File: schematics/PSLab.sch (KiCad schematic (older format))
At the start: 79 parts, among them J1 Programmer, J10 GND, J11 Vbus, J13 D+, J14 D-, J15 External Power, J16 I2C-2, J2 DoublePins, J5 Bluetooth, J6 I2C-1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

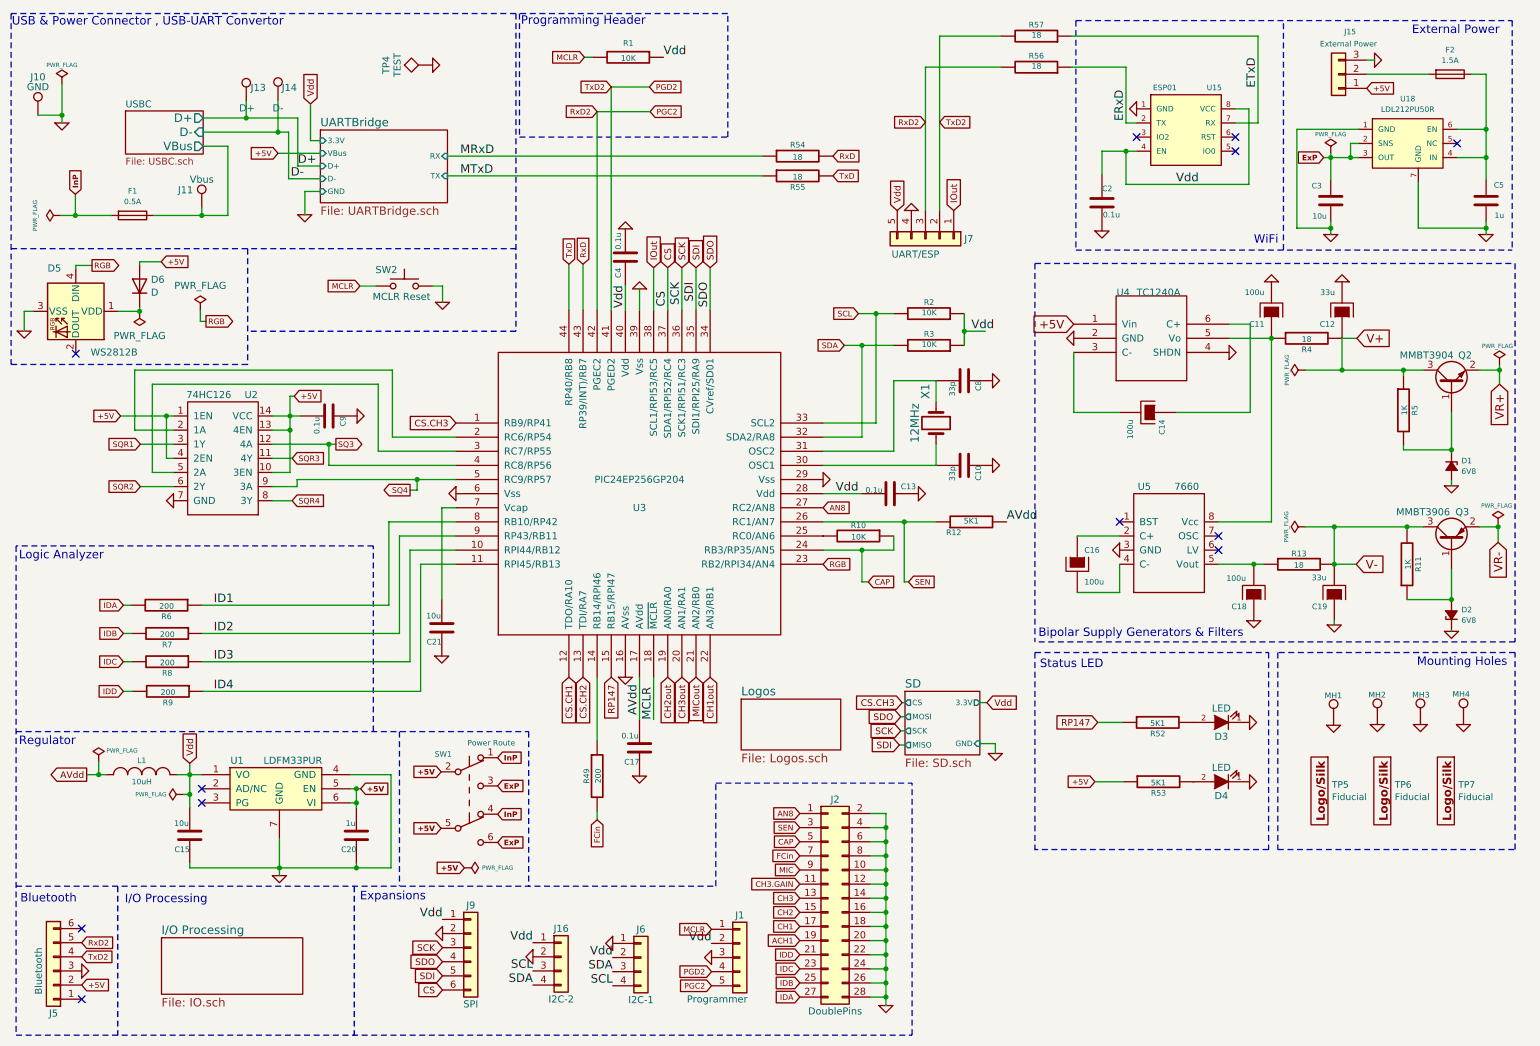
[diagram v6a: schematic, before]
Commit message: feat: bom generator and updated project to support bom generator
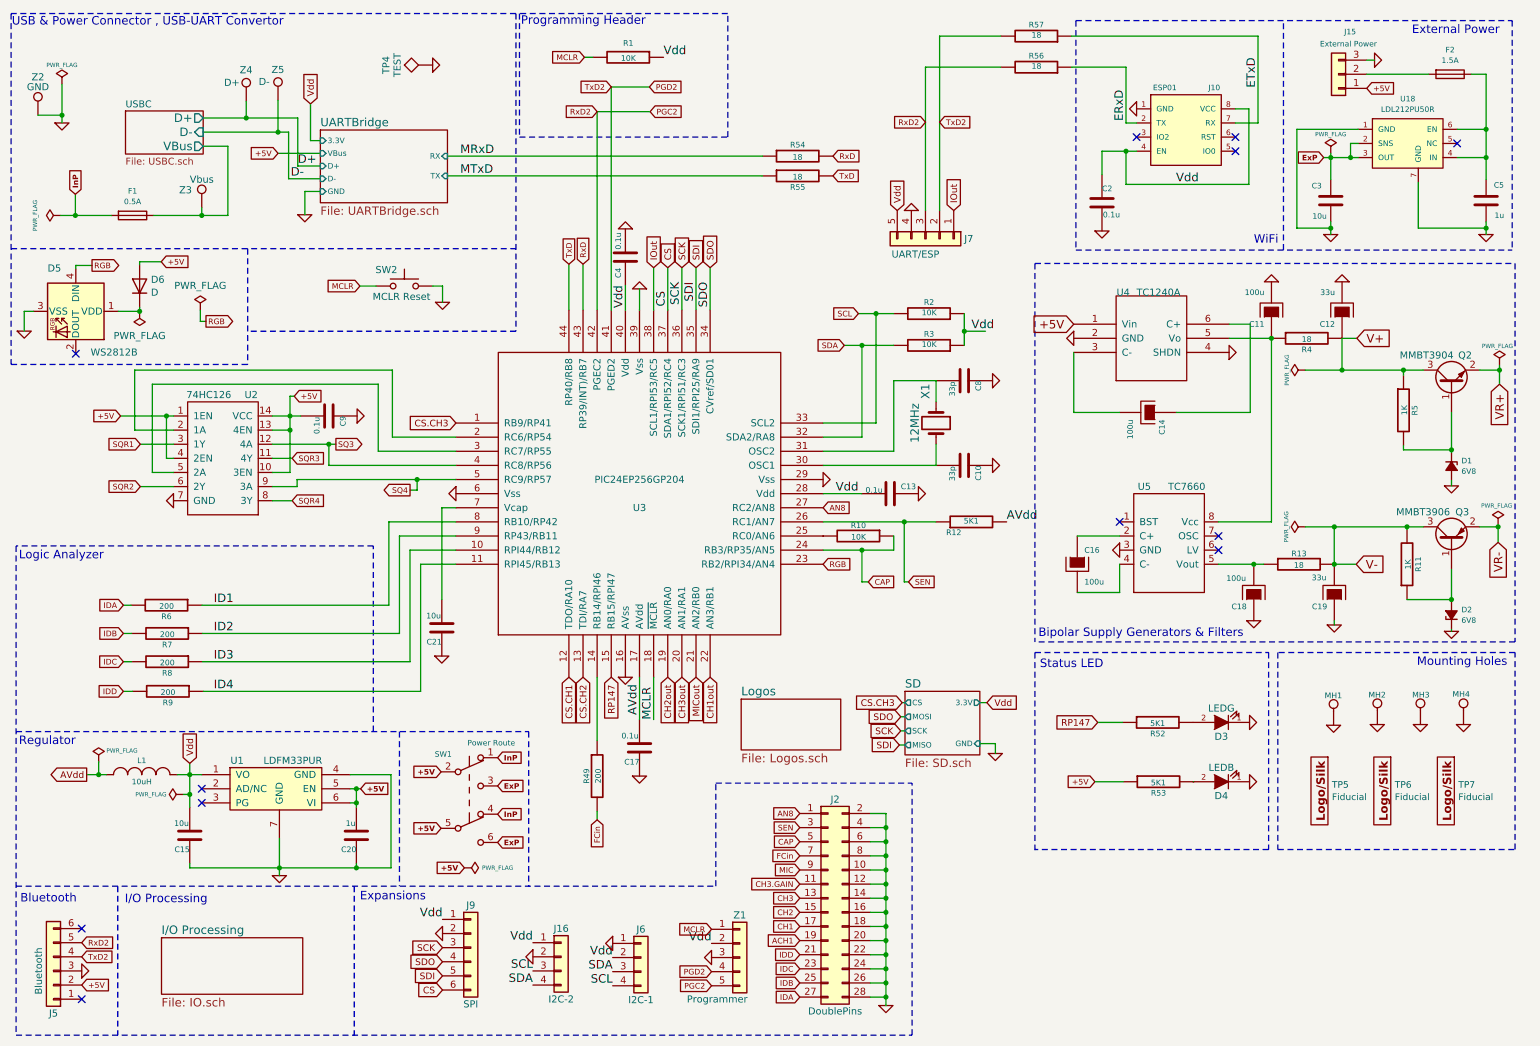
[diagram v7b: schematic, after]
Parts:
- C10, C8: Description (none) -> 16V 10%; Mfr No. (none) -> VJ0603A330JXJPW1BC; PartNumber (none) -> VJ0603A330JXJPW1BC; Price (none) -> 0.26
- C11, C14, C16, C18: Description (none) -> Tantalum 16V 6032-28; Mfr No. (none) -> F931C107KCC; PartNumber (none) -> F931C107KCC; Price (none) -> 1.29
- C12, C19: Description (none) -> Tantalum 16V 3528-21; Mfr No. (none) -> 293D336X9016B2TE3; PartNumber (none) -> 293D336X9016B2TE3; Price (none) -> 0.81
- C13, C17, C2, C4, C9: Description (none) -> 16V 10%; Mfr No. (none) -> C0603C104J4RACTU; PartNumber (none) -> C0603C104J4RACTU; Price (none) -> 0.15
- C15, C21, C3: Description (none) -> 16V 20%; Mfr No. (none) -> EMK107BC6106MA-T; PartNumber (none) -> EMK107BC6106MA-T; Price (none) -> 0.46
- C20, C5: Description (none) -> 16V 20%; Mfr No. (none) -> 0603YD105KAT2A; PartNumber (none) -> 0603YD105KAT2A; Price (none) -> 0.18
- D1, D2: Description (none) -> 6.8V Zener; Mfr No. (none) -> BZV55B6V8 L1; PartNumber (none) -> BZV55B6V8 L1; Price (none) -> 0.23
- D3: value LED -> LEDG; Description (none) -> Green 0805; Mfr No. (none) -> HSMQ-C170-T0000; PartNumber (none) -> HSMQ-C170-T0000; Price (none) -> 0.94
- D4: value LED -> LEDB; Description (none) -> Blue 0805; Mfr No. (none) -> HSMR-C170-R0000; PartNumber (none) -> HSMR-C170-R0000; Price (none) -> 0.85
- D5: Description (none) -> RGB LED with integrated controller; Mfr No. (none) -> WS2812B; PartNumber (none) -> WS2812B; Price (none) -> 3.35
- D6: Description (none) -> General Purpose diode; Mfr No. (none) -> LL4448 L0; PartNumber (none) -> LL4448 L0; Price (none) -> 0.11
- F1: Description (none) -> Hold 250mA, Trip 500mA; Mfr No. (none) -> 0ZCJ0025FF2E; PartNumber (none) -> 0ZCJ0025FF2E; Price (none) -> 0.11
- F2: Description (none) -> Hold 1A, Trip 1.8A; Mfr No. (none) -> 0ZCJ0100FF2E; PartNumber (none) -> 0ZCJ0100FF2E; Price (none) -> 0.17
- J10: renamed from U15; footprint Custom_Components:ESP-01 -> PSLab:ESP-01; Description (none) -> Straight female 2.54 mm 2row; Mfr No. (none) -> SSW-104-01-T-D; PartNumber (none) -> SSW-104-01-T-D; Price (none) -> 0.98
- J15: Description (none) -> Straight female 2.54 mm 1row; Mfr No. (none) -> SSW-103-01-T-S; PartNumber (none) -> SSW-103-01-T-S; Price (none) -> 0.5
- J16, J6: Description (none) -> Straight female 2.54 mm 1row; Mfr No. (none) -> SSW-104-01-T-S; PartNumber (none) -> SSW-104-01-T-S; Price (none) -> 0.63
- J2: Description (none) -> Straight female 2.54 mm 2row; Mfr No. (none) -> SSW-114-01-T-D; PartNumber (none) -> SSW-114-01-T-D; Price (none) -> 2.28
- J5, J9: Description (none) -> Straight female 2.54 mm 1row; Mfr No. (none) -> SSW-106-01-T-S; PartNumber (none) -> SSW-106-01-T-S; Price (none) -> 0.68
- J7: Description (none) -> Straight female 2.54 mm 1row; Mfr No. (none) -> SSW-105-01-T-S; PartNumber (none) -> SSW-105-01-T-S; Price (none) -> 0.65
- L1: Description (none) -> 300-500 mA Shielded; Mfr No. (none) -> MLZ1608N100LT000; PartNumber (none) -> MLZ1608N100LT000; Price (none) -> 0.17
- MH1, MH2, MH3, MH4: Description (none) -> M3 Nut - 3.2mm_M3.5_DIN965; Mfr No. (none) -> 9774030360R; PartNumber (none) -> 9774030360R; Price (none) -> 2.86
- Q2: Description (none) -> 45V Vce, 0.8A Ic, NPN, SOT-23; Mfr No. (none) -> MMBT3904,215; PartNumber (none) -> MMBT3904,215; Price (none) -> 0.1
- Q3: Description (none) -> 45V Vce, 0.8A Ic, PNP, SOT-23; Mfr No. (none) -> MMBT3906-7-F; PartNumber (none) -> MMBT3906-7-F; Price (none) -> 0.11
- R1, R10, R2, R3: Description (none) -> 1/16W 5%; Mfr No. (none) -> RR0816P-103-D; PartNumber (none) -> RR0816P-103-D; Price (none) -> 0.12
- R11, R5: Description (none) -> 1/16W 5%; Mfr No. (none) -> RR0816P-102-D; PartNumber (none) -> RR0816P-102-D; Price (none) -> 0.12
- R12, R52, R53: Description (none) -> 1/16W 5%; Mfr No. (none) -> RR0816P-512-D; PartNumber (none) -> RR0816P-512-D; Price (none) -> 0.1
- R13, R4, R54, R55, R56, R57: Description (none) -> 1/16W 5%; Mfr No. (none) -> RR0816Q-180-D; PartNumber (none) -> RR0816Q-180-D; Price (none) -> 0.1
- R49, R6, R7, R8, R9: Description (none) -> 1/16W 5%; Mfr No. (none) -> RR0816P-201-D; PartNumber (none) -> RR0816P-201-D; Price (none) -> 0.1
- SW1: Description (none) -> Slide Switches DPDT THRU HOLE; PartNumber (none) -> JS202011CQN; Price (none) -> 0.43
- SW2: Description (none) -> Tactile Switches SPST SMD; Mfr No. (none) -> B3U-1000P; PartNumber (none) -> B3U-1000P; Price (none) -> 0.56
- U1: Description (none) -> DFN-6-1EP_3x3mm_Pitch0.95mm; Mfr No. (none) -> LDFM33PUR; PartNumber (none) -> LDFM33PUR; Price (none) -> 0.72
- U18: Description (none) -> DFN-6-1EP_3x3mm_Pitch0.95mm; Mfr No. (none) -> LDL212PU50R; PartNumber (none) -> LDL212PU50R; Price (none) -> 0.51
- U2: Description (none) -> SOIC 14; Mfr No. (none) -> 74HC126D(BJ); PartNumber (none) -> 74HC126D(BJ); Price (none) -> 0.42
- U3: Description (none) -> TQFP 44; Mfr No. (none) -> PIC24EP256GP204-I/PT; PartNumber (none) -> PIC24EP256GP204-I/PT; Price (none) -> 3.35
- U4: Description (none) -> SOT-23-6; Mfr No. (none) -> TC1240AECHTR; PartNumber (none) -> TC1240AECHTR; Price (none) -> 0.82
- U5: value 7660 -> TC7660; Description (none) -> SOIC 8; Mfr No. (none) -> TC7660SEOA713; PartNumber (none) -> TC7660SEOA713; Price (none) -> 0.90
- X1: Description (none) -> 18pF 30ppm; Mfr No. (none) -> ABM3-12.000MHZ-D2Y-T; PartNumber (none) -> ABM3-12.000MHZ-D2Y-T; Price (none) -> 0.78
- renumbered J1 to Z1, J10 to Z2, J11 to Z3, J13 to Z4, J14 to Z5

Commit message: refactor: corrected IC annotation order
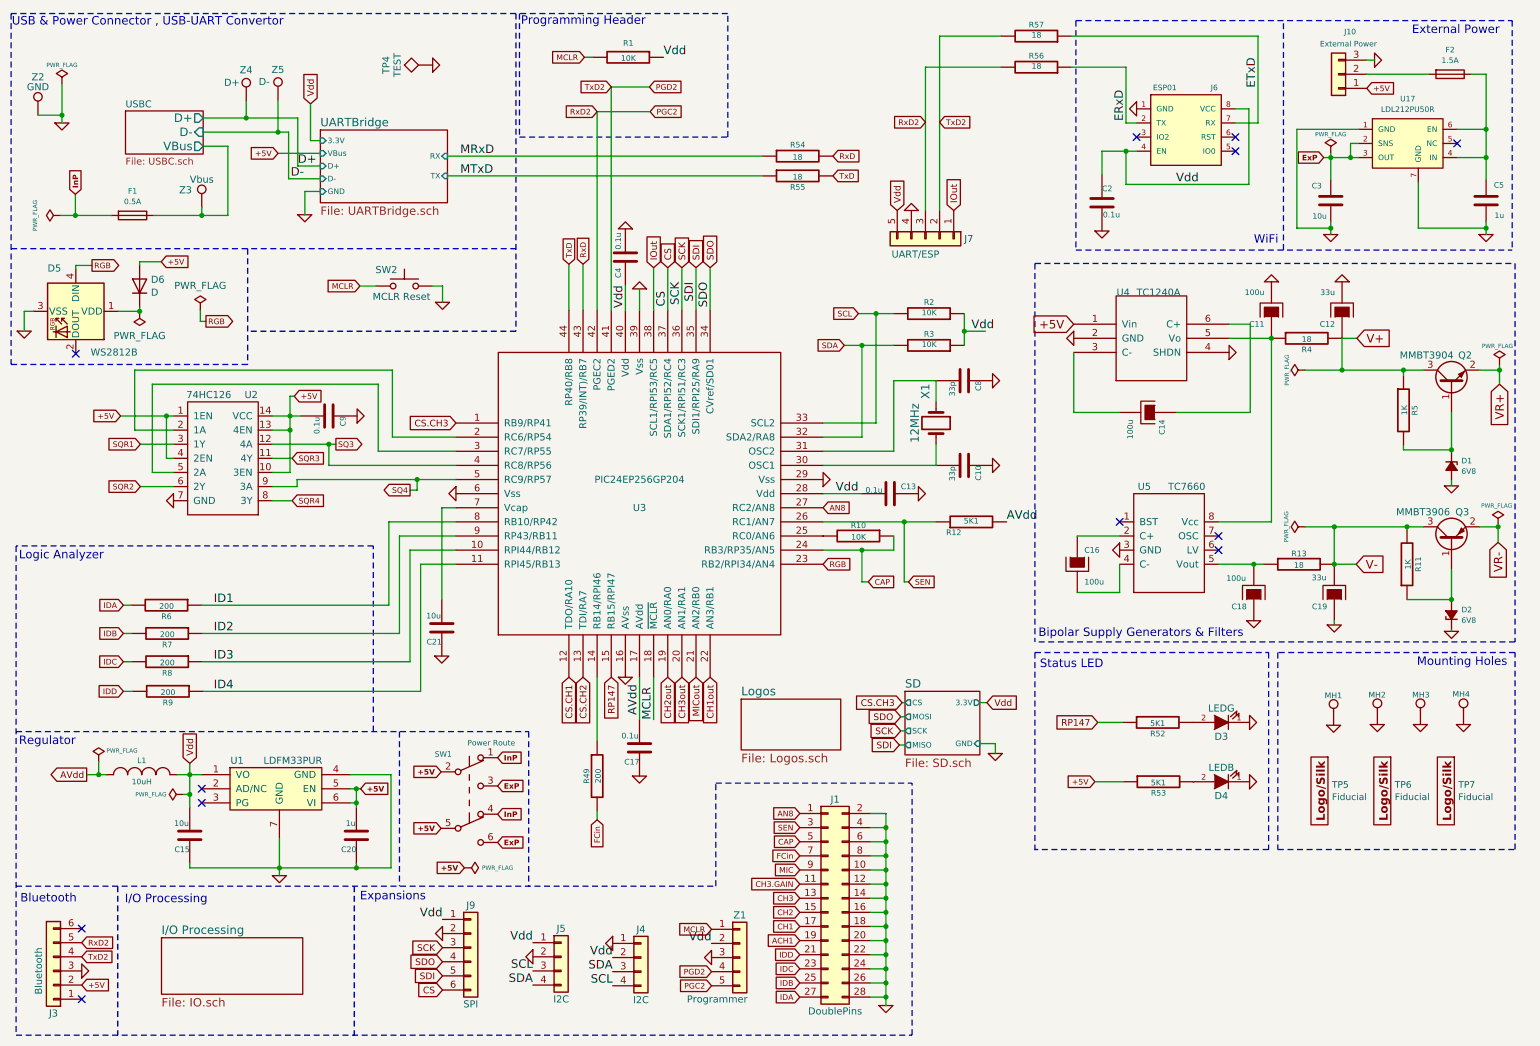
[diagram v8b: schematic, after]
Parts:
- J4: renamed from J6; value I2C-1 -> I2C
- J5: renamed from J16; value I2C-2 -> I2C
- U2: footprint Housings_SOIC:SOIC-14_3.9x8.7mm_Pitch1.27mm -> Package_SO:SOIC-14_3.9x8.7mm_P1.27mm
- U3: footprint Housings_QFP:TQFP-44_10x10mm_Pitch0.8mm -> Package_QFP:TQFP-44_10x10mm_P0.8mm
- U4: footprint TO_SOT_Packages_SMD:SOT-23-6 -> Package_TO_SOT_SMD:SOT-23-6
- U5: footprint Housings_SOIC:SOIC-8_3.9x4.9mm_Pitch1.27mm -> Package_SO:SOIC-8_3.9x4.9mm_P1.27mm
- renumbered J2 to J1, J15 to J10, J5 to J3, J10 to J6, U18 to U17
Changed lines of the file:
@@
 F 0 "U4" H 8375 3125 50  0000 C CNN
 F 1 "TC1240A" H 8625 3125 50  0000 C CNN
-F 2 "TO_SOT_Packages_SMD:SOT-23-6" H 8575 3000 50  0001 C CNN
+F 2 "Package_TO_SOT_SMD:SOT-23-6" H 8575 3000 50  0001 C CNN
 F 3 "https://eu.mouser.com/datasheet/2/268/21516c-4387.pdf" H 8575 2600 50  0001 C CNN
 F 4 "SOT-23-6" H 8575 2800 50  0001 C CNN "Description"
@@
 F 0 "U5" H 8525 4650 50  0000 C CNN
 F 1 "TC7660" H 8825 4650 50  0000 C CNN
-F 2 "Housings_SOIC:SOIC-8_3.9x4.9mm_Pitch1.27mm" H 8700 4250 50  0001 C CNN
+F 2 "Package_SO:SOIC-8_3.9x4.9mm_P1.27mm" H 8700 4250 50  0001 C CNN
 F 3 "https://eu.mouser.com/datasheet/2/268/21467B-1180369.pdf" H 8700 4250 50  0001 C CNN
 F 4 "SOIC 8" H 8700 4250 50  0001 C CNN "Description"
@@
 F 0 "U2" H 2200 4300 50  0000 C CNN
 F 1 "74HC126" H 1900 4300 50  0000 C CNN
-F 2 "Housings_SOIC:SOIC-14_3.9x8.7mm_Pitch1.27mm" V 1975 3575 50  0001 C CNN
+F 2 "Package_SO:SOIC-14_3.9x8.7mm_P1.27mm" V 1975 3575 50  0001 C CNN
 F 3 "https://eu.mouser.com/datasheet/2/408/74HC126D_datasheet_en_20160804-959200.pdf" V 1925 3575 50  0001 C CNN
 F 4 "SOIC 14" H 1800 3750 50  0001 C CNN "Description"
@@
 F 0 "U3" H 4950 3800 50  0000 C CNN
 F 1 "PIC24EP256GP204" H 4950 4000 50  0000 C CNN
-F 2 "Housings_QFP:TQFP-44_10x10mm_Pitch0.8mm" H 4950 3900 50  0001 C CNN
+F 2 "Package_QFP:TQFP-44_10x10mm_P0.8mm" H 4950 3900 50  0001 C CNN
 F 3 "https://eu.mouser.com/datasheet/2/268/70000657H-277982.pdf" H 4950 3900 50  0001 C CNN
 F 4 "TQFP 44" H 4950 3900 50  0001 C CNN "Description"
@@
 MCLR
 $Comp
-L PSLab-rescue:Conn_01x04 J6
+L PSLab-rescue:Conn_01x04 J4
 U 1 1 5A584DF9
 P 4960 7185
-F 0 "J6" H 4960 7385 50  0000 C CNN
-F 1 "I2C-1" H 4960 6885 50  0000 C CNN
+F 0 "J4" H 4960 7385 50  0000 C CNN
+F 1 "I2C" H 4960 6885 50  0000 C CNN
 F 2 "Pin_Headers:Pin_Header_Straight_1x04_Pitch2.54mm" H 4960 7185 50  0001 C CNN
 F 3 "https://eu.mouser.com/datasheet/2/527/ssw_th-1507658.pdf" H 4960 7185 50  0001 C CNN
@@
 Text Label 5460 7085 2    60   ~ 0
 Vdd
-$Comp
-L PSLab-rescue:Conn_01x04 J16
-U 1 1 5AD47B2C
-P 4395 7180
-F 0 "J16" H 4395 7380 50  0000 C CNN
-F 1 "I2C-2" H 4395 6880 50  0000 C CNN
-F 2 "Pin_Headers:Pin_Header_Straight_1x04_Pitch2.54mm" H 4395 7180 50  0001 C CNN
-F 3 "https://eu.mouser.com/datasheet/2/527/ssw_th-1507658.pdf" H 4395 7180 50  0001 C CNN
-F 4 "Straight female 2.54 mm 1row" H 4395 7180 50  0001 C CNN "Description"
-F 5 "SSW-104-01-T-S" H 4395 7180 50  0001 C CNN "Mfr No."
-F 6 "0.63" H 4395 7180 50  0001 C CNN "Price"
-F 7 "SSW-104-01-T-S" H 4395 7180 50  0001 C CNN "PartNumber"
-	1    4395 7180
-	1    0    0    -1
-$EndComp
 $Comp
 L PSLab-rescue:GND-RESCUE-proto1 #PWR044
@@
 SEN
 $Comp
-L PSLab-rescue:Conn_02x14_Odd_Even J2
+L PSLab-rescue:Conn_02x14_Odd_Even J1
 U 1 1 5ADBCA02
 P 6285 6765
-F 0 "J2" H 6335 7465 50  0000 C CNN
+F 0 "J1" H 6335 7465 50  0000 C CNN
 F 1 "DoublePins" H 6335 5965 50  0000 C CNN
 F 2 "Pin_Headers:Pin_Header_Straight_2x14_Pitch2.54mm" H 6285 6765 50  0001 C CNN
@@
 Vdd
 $Comp
-L PSLab-rescue:Conn_01x06 J5
+L PSLab-rescue:Conn_01x06 J3
 U 1 1 5ADB5C89
 P 800 7280
-F 0 "J5" H 800 7580 50  0000 C CNN
+F 0 "J3" H 800 7580 50  0000 C CNN
 F 1 "Bluetooth" V 905 7280 50  0000 C CNN
 F 2 "Pin_Headers:Pin_Header_Straight_1x06_Pitch2.54mm" H 800 7280 50  0001 C CNN
@@
 	1850 4690 3175 4690
 $Comp
-L PSLab-rescue:ESP01-PSLab J10
+L PSLab-rescue:ESP01-PSLab J6
 U 1 1 5EB1EA49
 P 8820 1325
-F 0 "J10" H 9020 1625 39  0000 C CNN
+F 0 "J6" H 9020 1625 39  0000 C CNN
 F 1 "ESP01" H 8670 1625 39  0000 C CNN
 F 2 "PSLab:ESP-01" H 8820 1325 60  0001 C CNN
@@
 ExP
 $Comp
-L Connector_Generic:Conn_01x03 J15
+L Connector_Generic:Conn_01x03 J10
 U 1 1 5EF478E2
 P 9900 930
-F 0 "J15" H 9818 629 39  0000 C CNN
+F 0 "J10" H 9818 629 39  0000 C CNN
 F 1 "External Power" H 9830 715 39  0000 C CNN
 F 2 "Connector_PinSocket_2.54mm:PinSocket_1x03_P2.54mm_Vertical" H 9900 930 50  0001 C CNN
@@
 $EndComp
 $Comp
-L PSLab:LDL212PU50R U18
+L PSLab:LDL212PU50R U17
 U 1 1 5EF1AD6F
 P 10390 1420
-F 0 "U18" H 10390 1736 39  0000 C CNN
+F 0 "U17" H 10390 1736 39  0000 C CNN
 F 1 "LDL212PU50R" H 10390 1661 39  0000 C CNN
 F 2 "Package_DFN_QFN:DFN-6-1EP_3x3mm_P0.95mm_EP1.7x2.6mm" H 10390 1420 39  0001 C CNN
@@
 $EndComp
 Connection ~ 1410 2609
+$Comp
+L PSLab-rescue:Conn_01x04 J5
+U 1 1 5AD47B2C
+P 4395 7180
+F 0 "J5" H 4395 7380 50  0000 C CNN
+F 1 "I2C" H 4395 6880 50  0000 C CNN
+F 2 "Pin_Headers:Pin_Header_Straight_1x04_Pitch2.54mm" H 4395 7180 50  0001 C CNN
+F 3 "https://eu.mouser.com/datasheet/2/527/ssw_th-1507658.pdf" H 4395 7180 50  0001 C CNN
+F 4 "Straight female 2.54 mm 1row" H 4395 7180 50  0001 C CNN "Description"
+F 5 "SSW-104-01-T-S" H 4395 7180 50  0001 C CNN "Mfr No."
+F 6 "0.63" H 4395 7180 50  0001 C CNN "Price"
+F 7 "SSW-104-01-T-S" H 4395 7180 50  0001 C CNN "PartNumber"
+	1    4395 7180
+	1    0    0    -1
+$EndComp
 $EndSCHEMATC
